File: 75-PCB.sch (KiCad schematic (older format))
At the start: 324 parts, among them J1 AVR-ISP-6, Q1 2N7002, SW1 SW_Push, U1 AT90USB1286-AU, U2 PRTR5V0U2X, Y1 16MHz

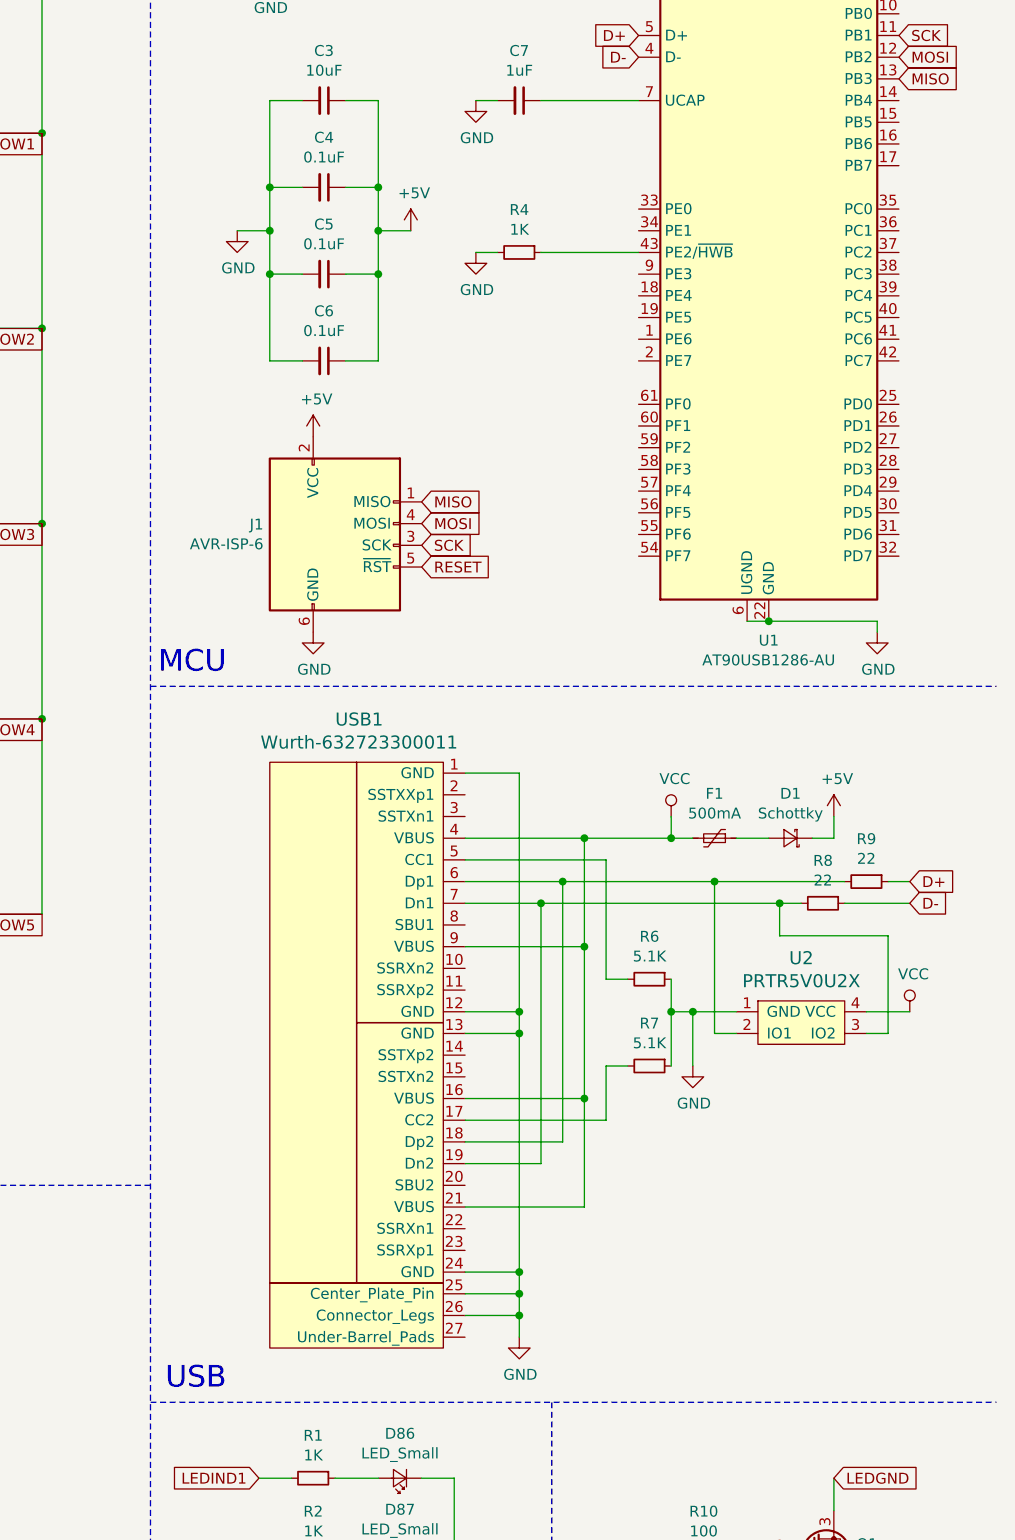
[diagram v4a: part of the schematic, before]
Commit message: Changed USB connector
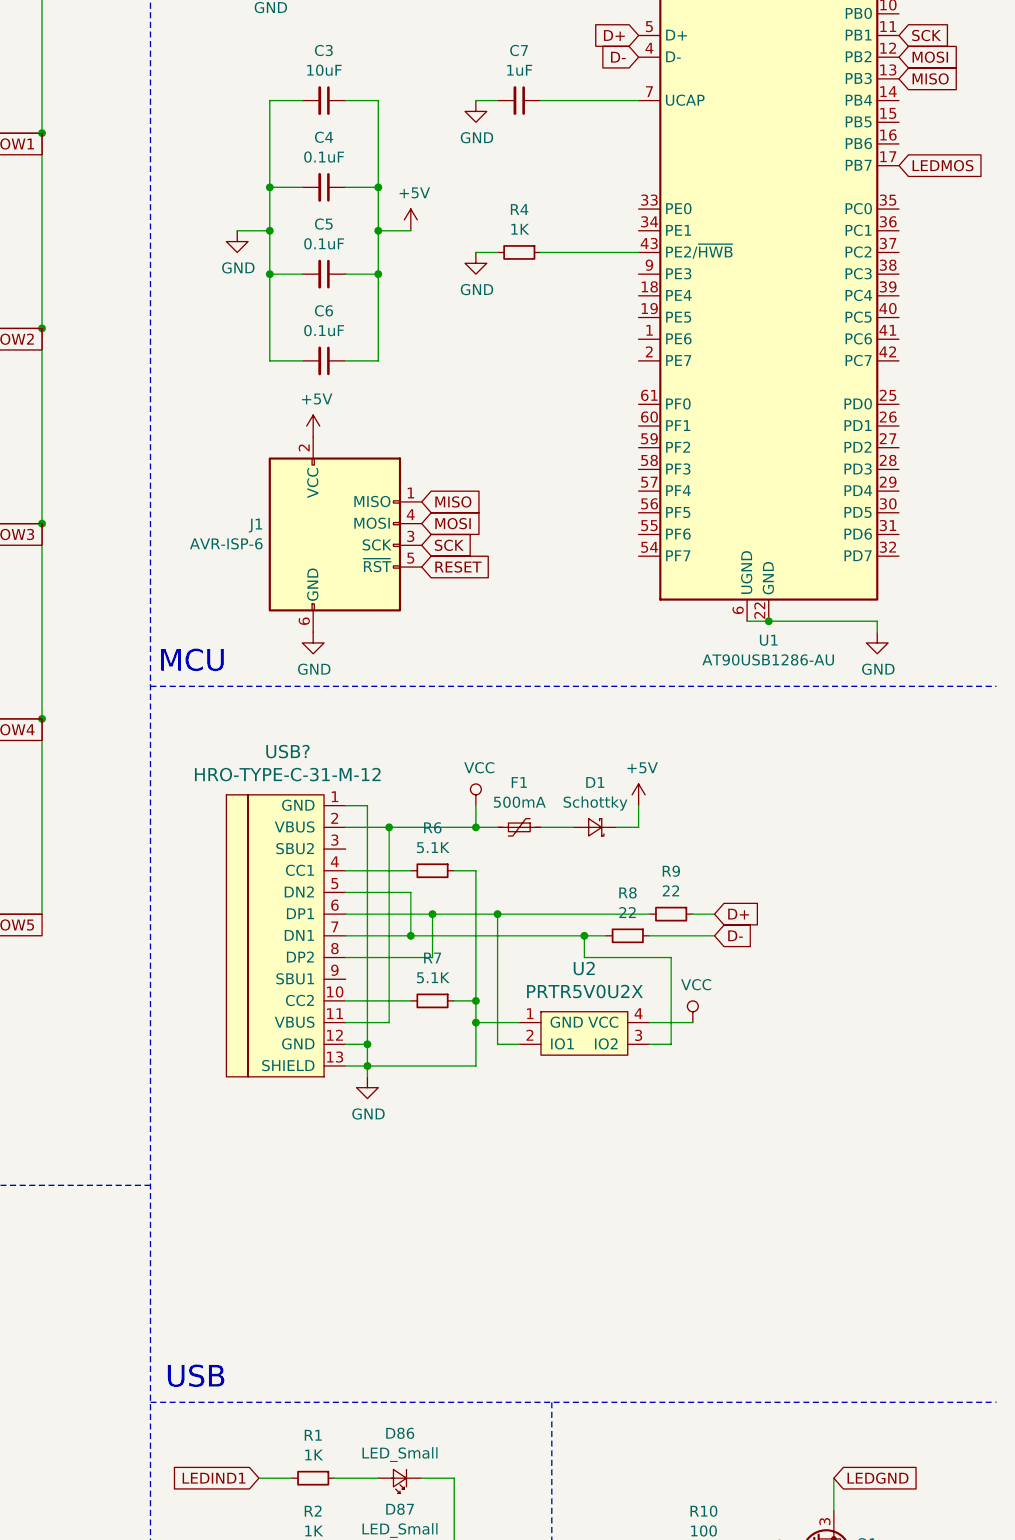
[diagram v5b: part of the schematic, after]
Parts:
- removed USB1: Wurth-632723300011, Type-C:Wurth-632723300011-HandSoldering, symbol Type-C:Wurth-632723300011
- added USB?: HRO-TYPE-C-31-M-12, symbol Type-C:HRO-TYPE-C-31-M-12
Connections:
- net GND: now also USB?.1 (GND), USB?.12 (GND), USB?.13 (SHIELD)
- net LEDMOS: now also U1.17 (PB7)
- net VCC: now also USB?.11 (VBUS), USB?.2 (VBUS)
- net at R7.2: now also USB?.10 (CC2)
- net at R9.2, U2.2 (IO1): now also USB?.6 (DP1), USB?.8 (DP2)
- net at R8.2, U2.3 (IO2): now also USB?.5 (DN2), USB?.7 (DN1)
- net at R6.2: now also USB?.4 (CC1)
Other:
- moved on the sheet: D1, F1, R6, R7, R8, R9, U2

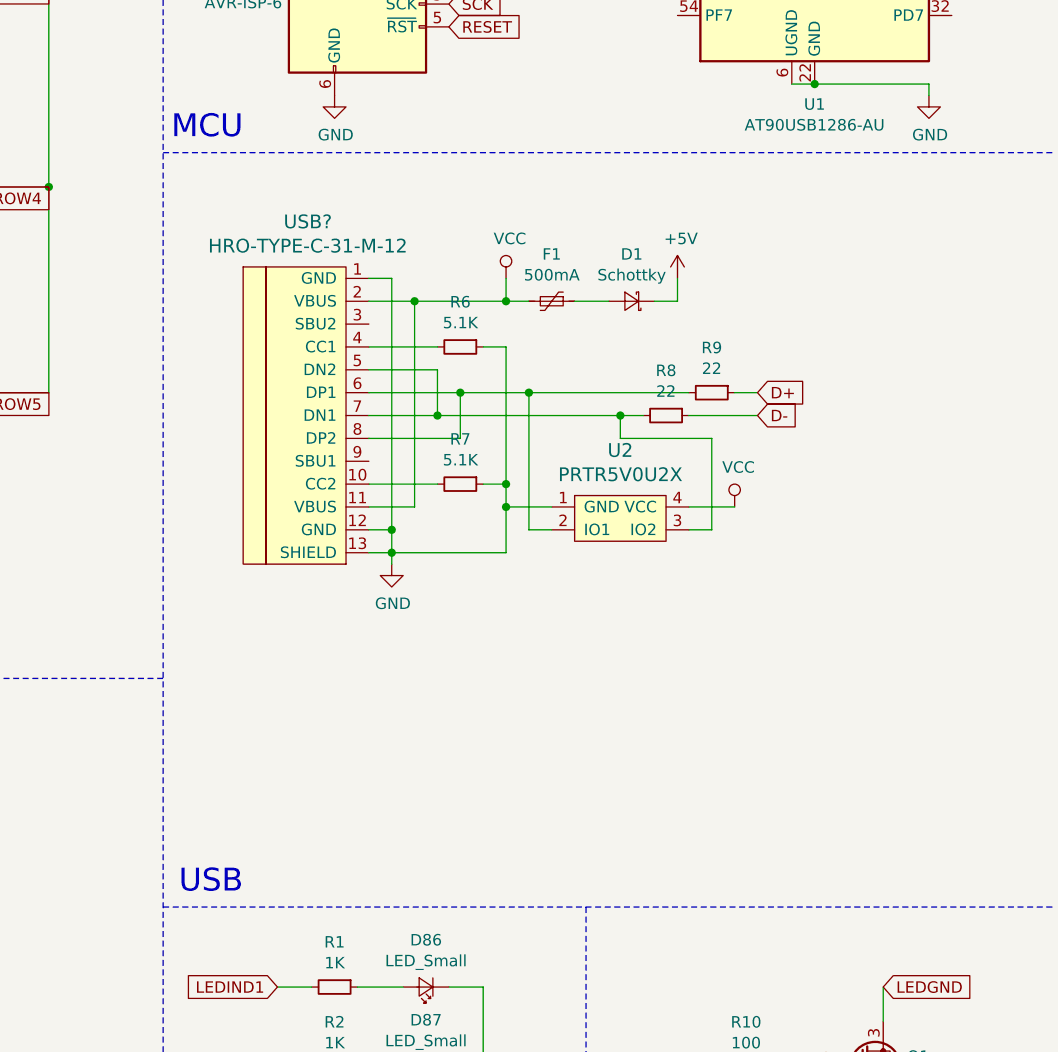
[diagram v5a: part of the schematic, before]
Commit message: Changed USB connector
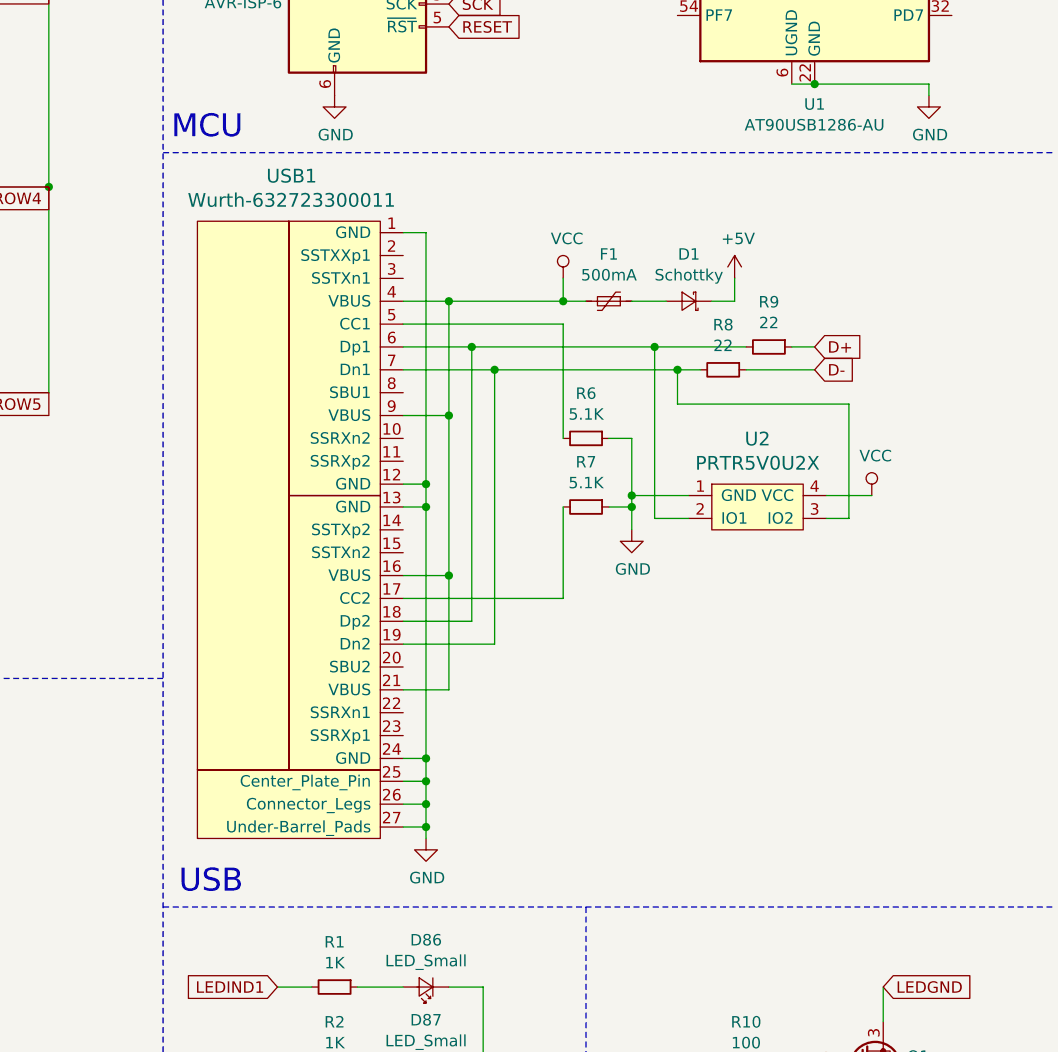
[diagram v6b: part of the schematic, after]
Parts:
- removed USB?: HRO-TYPE-C-31-M-12, symbol Type-C:HRO-TYPE-C-31-M-12
- added USB1: Wurth-632723300011, Type-C:Wurth-632723300011, symbol Type-C:Wurth-632723300011
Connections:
- net GND: now also USB1.1 (GND), USB1.12 (GND), USB1.13 (GND), USB1.24 (GND), USB1.25 (Center_Plate_Pin), USB1.26 (Connector_Legs), USB1.27 (Under-Barrel_Pads)
- net VCC: now also USB1.16 (VBUS), USB1.21 (VBUS), USB1.4 (VBUS), USB1.9 (VBUS)
- net at R9.2, U2.2 (IO1): now also USB1.18 (Dp2), USB1.6 (Dp1)
- net at R8.2, U2.3 (IO2): now also USB1.19 (Dn2), USB1.7 (Dn1)
- net at R6.2: now also USB1.5 (CC1)
- net at R7.2: now also USB1.17 (CC2)
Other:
- moved on the sheet: D1, F1, R6, R7, R8, R9, U2

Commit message: Updated switch footprints
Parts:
- MX_ENTER2: footprint MX_Only:MXOnly-ISO-ReversedStabilizers -> MX_Only:MXOnly-ISO-ROTATED-ReversedStabilizers
- MX_LALT2, MX_LCTRL2: footprint MX_Only:MXOnly-1.5U -> MX_Only:MXOnly-1.5U-FLIPPED
- MX_LWIN2: footprint MX_Only:MXOnly-1U -> MX_Only:MXOnly-1U-FLIPPED
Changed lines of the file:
@@
 F 0 "MX_ENTER2" H 9632 4374 60  0000 C CNN
 F 1 "MX-LED" H 9632 4300 20  0000 C CNN
-F 2 "MX_Only:MXOnly-ISO-ReversedStabilizers" H 8925 4125 60  0001 C CNN
+F 2 "MX_Only:MXOnly-ISO-ROTATED-ReversedStabilizers" H 8925 4125 60  0001 C CNN
 F 3 "" H 8925 4125 60  0001 C CNN
 	1    9550 4150
@@
 	3700 6300 2400 6300
 $Comp
-L MX_Alps_Hybrid:MX-LED MX_LCTRL2
-U 1 1 5EB2F6D3
-P 1250 6850
-F 0 "MX_LCTRL2" H 1332 7074 60  0000 C CNN
-F 1 "MX-LED" H 1332 7000 20  0000 C CNN
-F 2 "MX_Only:MXOnly-1.5U" H 625 6825 60  0001 C CNN
-F 3 "" H 625 6825 60  0001 C CNN
-	1    1250 6850
-	1    0    0    -1
-$EndComp
-$Comp
 L MX_Alps_Hybrid:MX-LED MX_LALT2
 U 1 1 5EB62996
@@
 F 0 "MX_LALT2" H 2632 7074 60  0000 C CNN
 F 1 "MX-LED" H 2632 7000 20  0000 C CNN
-F 2 "MX_Only:MXOnly-1.5U" H 1925 6825 60  0001 C CNN
+F 2 "MX_Only:MXOnly-1.5U-FLIPPED" H 1925 6825 60  0001 C CNN
 F 3 "" H 1925 6825 60  0001 C CNN
 	1    2550 6850
@@
 	2700 6800 2700 5900
 Connection ~ 2700 5900
-Wire Wire Line
-	1400 6800 1400 5900
-Connection ~ 1400 5900
-Wire Wire Line
-	1200 7000 1200 6100
-Connection ~ 1200 6100
 $Comp
 L MX_Alps_Hybrid:MX-LED MX_RCTRL2
@@
 F 0 "MX_LWIN2" H 1982 7074 60  0000 C CNN
 F 1 "MX-LED" H 1982 7000 20  0000 C CNN
-F 2 "MX_Only:MXOnly-1U" H 1275 6825 60  0001 C CNN
+F 2 "MX_Only:MXOnly-1U-FLIPPED" H 1275 6825 60  0001 C CNN
 F 3 "" H 1275 6825 60  0001 C CNN
 	1    1900 6850
@@
 Connection ~ 1900 6050
 Wire Wire Line
-	1250 6950 1250 6050
-Connection ~ 1250 6050
-Wire Wire Line
 	2550 6950 2550 6050
 Connection ~ 2550 6050
@@
 Wire Wire Line
 	1350 5050 1350 4150
-Connection ~ 1350 5950
 Wire Wire Line
 	1350 5950 1350 5050
-Wire Wire Line
-	1350 6850 1350 5950
 $Comp
 L power:+5V #PWR0119
@@
 Wire Wire Line
 	13900 7150 13900 6750
+Connection ~ 1350 5950
+Connection ~ 1250 6050
+Connection ~ 1200 6100
+Connection ~ 1400 5900
+Wire Wire Line
+	1350 6850 1350 5950
+Wire Wire Line
+	1250 6950 1250 6050
+Wire Wire Line
+	1200 7000 1200 6100
+Wire Wire Line
+	1400 6800 1400 5900
+$Comp
+L MX_Alps_Hybrid:MX-LED MX_LCTRL2
+U 1 1 5EB2F6D3
+P 1250 6850
+F 0 "MX_LCTRL2" H 1332 7074 60  0000 C CNN
+F 1 "MX-LED" H 1332 7000 20  0000 C CNN
+F 2 "MX_Only:MXOnly-1.5U-FLIPPED" H 625 6825 60  0001 C CNN
+F 3 "" H 625 6825 60  0001 C CNN
+	1    1250 6850
+	1    0    0    -1
+$EndComp
 $EndSCHEMATC
